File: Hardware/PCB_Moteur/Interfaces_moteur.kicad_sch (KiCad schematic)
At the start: 53 parts, among them J10 BM03B-GHS-TBT, J12 BM03B-GHS-TBT, J13 Conn_01x02, J14 Conn_01x02, J15 Conn_01x02, J16 Conn_01x02, J17 Conn_01x02, J2 Conn_01x02, J3 Conn_01x02, J4 Conn_01x02, J5 Conn_01x02, J6 BM03B-GHS-TBT, J9 BM03B-GHS-TBT, U1 MCP1802T-5002I/OT, U4 LSF0204PWR, U8 ISOW1044

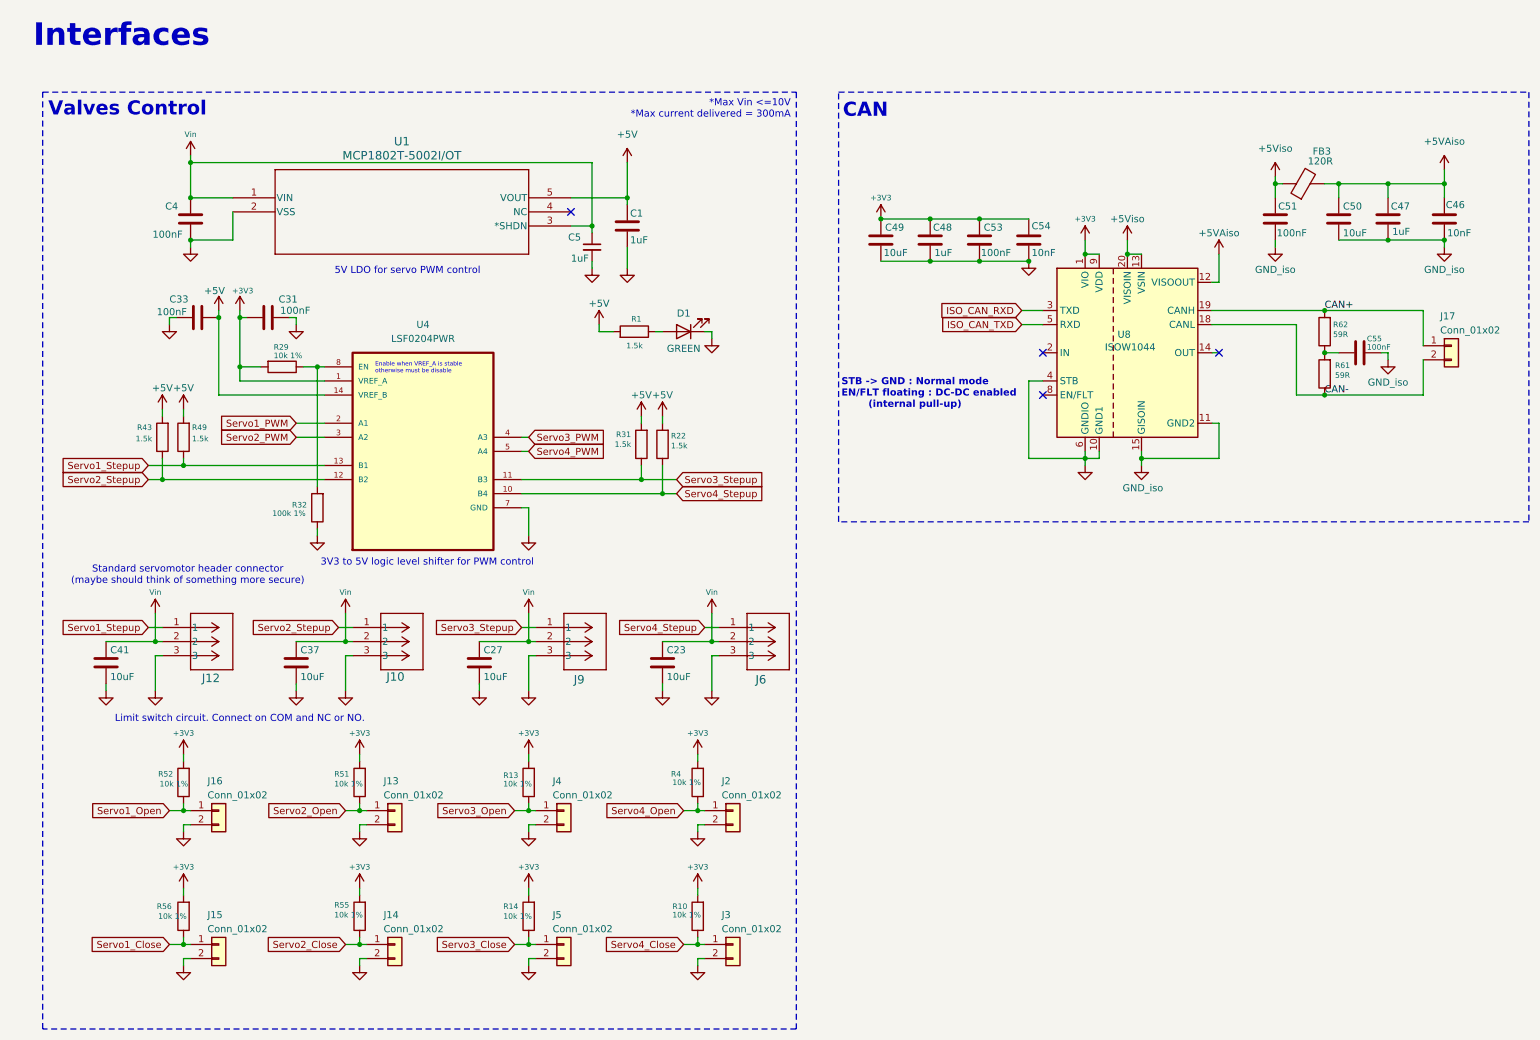
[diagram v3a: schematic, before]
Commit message: wip(moteur): add jack connector + fix dump valve
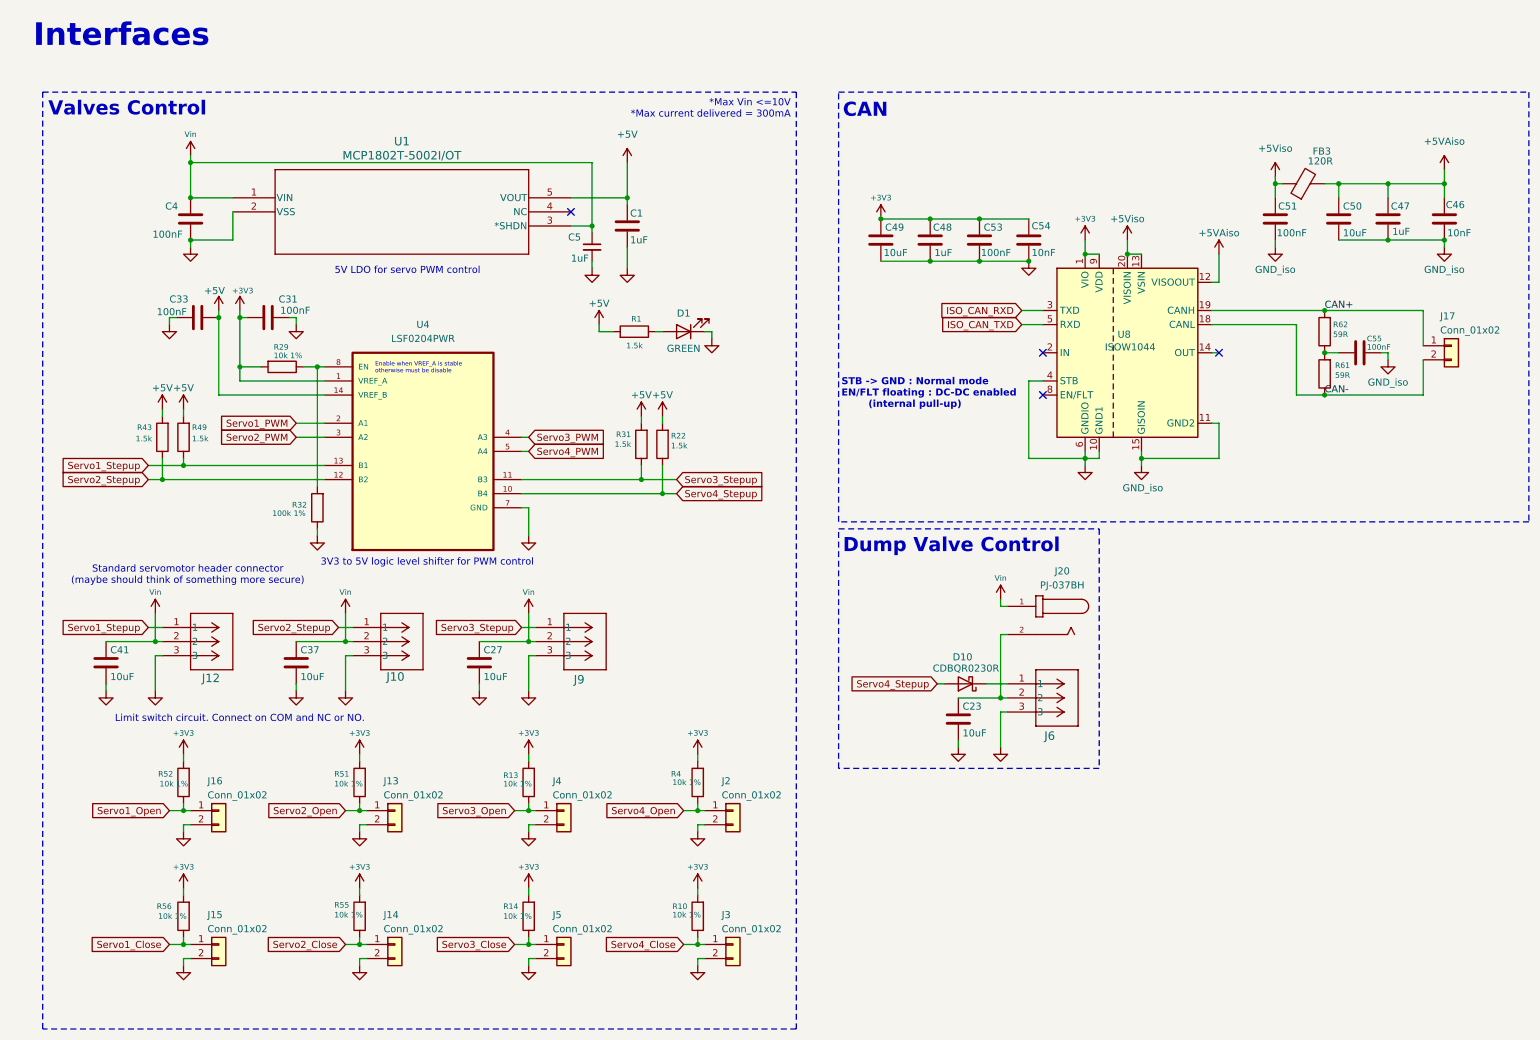
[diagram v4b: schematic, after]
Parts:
- added D10: CDBQR0230R, Diode_SMD:D_0603_1608Metric, symbol Diode:BAT54J
- added J20: PJ-037BH, pcb_moteur:SAMESKY_PJ-037BH, symbol pcb_moteur:PJ-037BH
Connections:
- net Servo4_Stepup: now also D10.2 (A); no longer J6.1
- net Vin: now also J20.1; no longer C23.1, J6.2
- new net: C23.1, J20.2, J6.2
- new net: D10.1 (K), J6.1
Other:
- note added: "Dump Valve Control"
- moved on the sheet: C23, J6

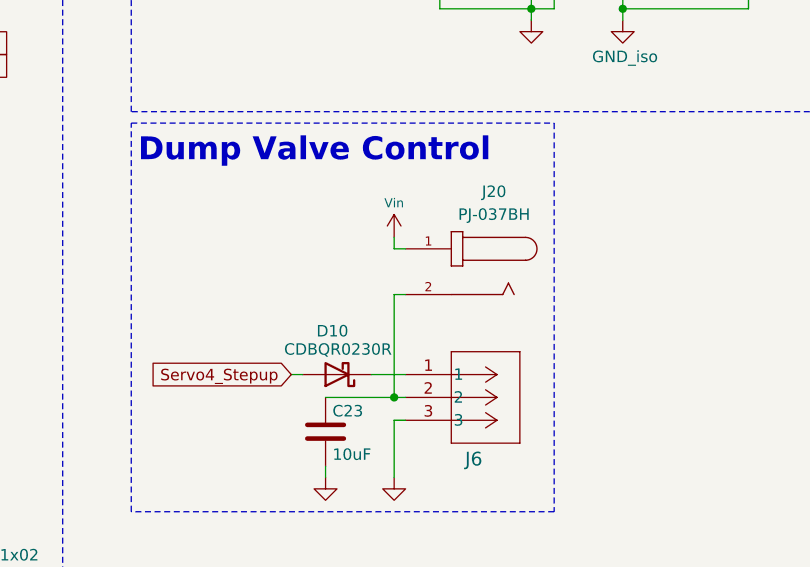
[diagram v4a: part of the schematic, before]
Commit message: Fix : connect all nets and fix dump valve kill
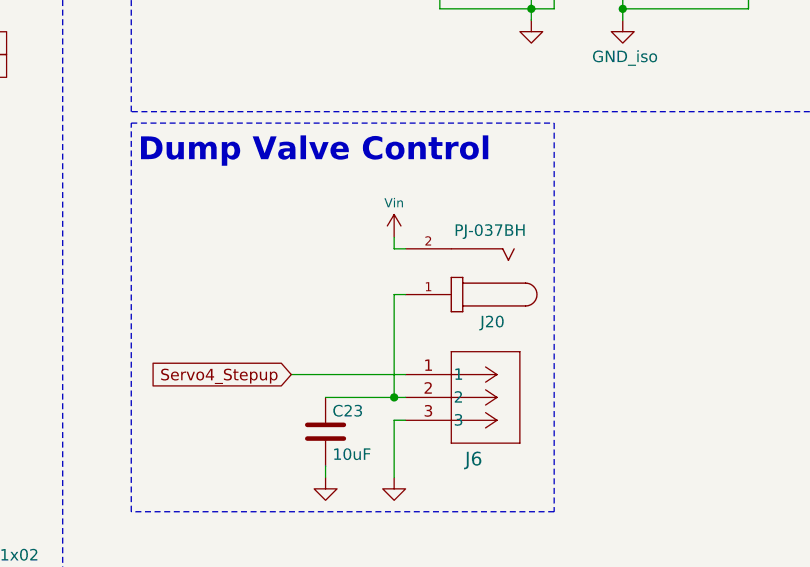
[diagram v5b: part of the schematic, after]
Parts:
- removed D10: CDBQR0230R, Diode_SMD:D_0603_1608Metric, symbol Diode:BAT54J
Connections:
- net Servo4_Stepup: now also J6.1
- net Vin: now also J20.2; no longer J20.1
- net at C23.1, J6.2: now also J20.1; no longer J20.2
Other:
- moved on the sheet: J20
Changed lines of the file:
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@@
 	(wire
 		(pts
+			(xy 187.96 119.38) (xy 189.23 119.38)
+		)
+		(stroke
+			(width 0)
+			(type default)
+		)
+	)
+	(wire
+		(pts
 			(xy 102.87 128.27) (xy 102.87 134.62)
 		)
@@
 	(wire
 		(pts
+			(xy 187.96 124.46) (xy 189.23 124.46)
+		)
+		(stroke
+			(width 0)
+			(type default)
+		)
+	)
+	(wire
+		(pts
 			(xy 36.83 125.73) (xy 35.56 125.73)
 		)
@@
 	(wire
 		(pts
-			(xy 189.23 124.46) (xy 187.96 124.46)
-		)
-		(stroke
-			(width 0)
-			(type default)
-		)
-	)
-	(wire
-		(pts
 			(xy 73.66 182.88) (xy 72.39 182.88)
 		)
@@
 	(wire
 		(pts
-			(xy 176.53 133.35) (xy 177.8 133.35)
+			(xy 176.53 133.35) (xy 189.23 133.35)
 		)
 		(stroke
@@
 	(wire
 		(pts
-			(xy 187.96 119.38) (xy 189.23 119.38)
-		)
-		(stroke
-			(width 0)
-			(type default)
-		)
-	)
-	(wire
-		(pts
 			(xy 46.99 67.31) (xy 46.99 81.28)
 		)
@@
 	(wire
 		(pts
-			(xy 185.42 133.35) (xy 189.23 133.35)
-		)
-		(stroke
-			(width 0)
-			(type default)
-		)
-	)
-	(wire
-		(pts
 			(xy 102.87 156.21) (xy 102.87 154.94)
 		)
@@
 	(symbol
 		(lib_id "pcb_moteur:PJ-037BH")
-		(at 194.31 121.92 0)
-		(mirror y)
+		(at 194.31 121.92 180)
 		(unit 1)
 		(exclude_from_sim no)
@@
 		(dnp no)
 		(property "Reference" "J20"
-			(at 199.0697 113.03 0)
+			(at 198.882 127.508 0)
 			(effects
 				(font
@@
 		)
 		(property "Value" "PJ-037BH"
-			(at 199.0697 115.57 0)
+			(at 198.628 117.348 0)
 			(effects
 				(font
@@
 					(unit 1)
 				)
-			)
-		)
-	)
-	(symbol
-		(lib_id "Diode:BAT54J")
-		(at 181.61 133.35 180)
-		(unit 1)
-		(exclude_from_sim no)
-		(in_bom yes)
-		(on_board yes)
-		(dnp no)
-		(property "Reference" "D10"
-			(at 182.88 128.524 0)
-			(effects
-				(font
-					(size 1.27 1.27)
-				)
-				(justify left)
-			)
-		)
-		(property "Value" "CDBQR0230R"
-			(at 187.706 130.556 0)
-			(effects
-				(font
-					(size 1.27 1.27)
-				)
-				(justify left)
-			)
-		)
-		(property "Footprint" "Diode_SMD:D_0603_1608Metric"
-			(at 181.61 128.905 0)
-			(effects
-				(font
-					(size 1.27 1.27)
-				)
-				(hide yes)
-			)
-		)
-		(property "Datasheet" "https://www.digikey.ca/en/products/detail/bourns-inc/CD0603-B0340R/7796828"
-			(at 181.61 133.35 0)
-			(effects
-				(font
-					(size 1.27 1.27)
-				)
-				(hide yes)
-			)
-		)
-		(property "Description" "30V 200mA Schottky diode, SOD-323F"
-			(at 181.61 133.35 0)
-			(effects
-				(font
-					(size 1.27 1.27)
-				)
-				(hide yes)
-			)
-		)
-		(property "DigiKey_Part_Number" "CD0603-B0340RCT-ND"
-			(at 181.61 133.35 90)
-			(effects
-				(font
-					(size 1.27 1.27)
-				)
-				(hide yes)
-			)
-		)
-		(property "Manufacturer_Part_Number" "CD0603-B0340R"
-			(at 181.61 133.35 90)
-			(effects
-				(font
-					(size 1.27 1.27)
-				)
-				(hide yes)
-			)
-		)
-		(pin "2"
-		)
-		(pin "1"
-		)
-		(instances
-			(project "PCB_moteur"
-				(path "/b0d87684-7b1c-41d8-8358-755aa327573e/a8ed0c04-b51e-4eec-84d1-0b2303d57d27"
-					(reference "D10")
-					(unit 1)
-				)

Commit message: Fix : servo side connectors
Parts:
- J10, J12, J6, J9: footprint pcb_moteur:CONN_BM03B-GHS-TBT_JST -> CONN_BM03B-GHS-TBT_JST; DigiKey_Part_Number - -> 455-SM03B-GHS-TBCT-ND; Manufacturer_Part_Number - -> SM03B-GHS-TB
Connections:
- net Vin: now also J10.4 (Case), J12.4 (Case), J9.4 (Case)
- no-connect marks 4 -> 5

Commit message: fix : add polyfuses and fix 90 deg servo connectors
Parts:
- J10, J12, J6, J9: footprint CONN_BM03B-GHS-TBT_JST -> pcb_moteur:JST_SM03B-GHS-TB
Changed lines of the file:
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@@
 			)
 		)
-		(property "Footprint" "CONN_BM03B-GHS-TBT_JST"
+		(property "Footprint" "pcb_moteur:JST_SM03B-GHS-TB"
 			(at 104.14 123.19 0)
 			(effects
@@
 			)
 		)
-		(property "Footprint" "CONN_BM03B-GHS-TBT_JST"
+		(property "Footprint" "pcb_moteur:JST_SM03B-GHS-TB"
 			(at 36.83 123.19 0)
 			(effects
@@
 			)
 		)
-		(property "Footprint" "CONN_BM03B-GHS-TBT_JST"
+		(property "Footprint" "pcb_moteur:JST_SM03B-GHS-TB"
 			(at 189.23 133.35 0)
 			(effects
@@
 			)
 		)
-		(property "Footprint" "CONN_BM03B-GHS-TBT_JST"
+		(property "Footprint" "pcb_moteur:JST_SM03B-GHS-TB"
 			(at 71.12 123.19 0)
 			(effects

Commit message: fix : BOM errors, change cutoff freq for moteur, minor fixes for GSE
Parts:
- C1, C47, C48, C5: DigiKey_Part_Number 399-C0603C105K4RACTUCT-ND -> 1276-1029-1-ND; Manufacturer_Part_Number C0603C105K4RACTU -> CL21B105KBFNNNE
- J20: Manufacturer_Part_Number (none) -> PJ-037BH
- R1, R22, R31, R43, R49: DigiKey_Part_Number P1.5KDBCT-ND -> 311-1.50KCRCT-ND; Manufacturer_Part_Number ERA-3AEB152V -> RC0805FR-071K5L
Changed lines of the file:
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@@
 			)
 		)
-		(property "Datasheet" "https://www.digikey.ca/en/products/detail/kemet/C0603C105K4RACTU/2199788"
+		(property "Datasheet" "https://www.digikey.ca/en/products/detail/samsung-electro-mechanics/CL21B105KBFNNNE/3886687"
 			(at 114.3 54.61 0)
 			(effects
@@
 			)
 		)
-		(property "DigiKey_Part_Number" "399-C0603C105K4RACTUCT-ND"
+		(property "DigiKey_Part_Number" "1276-1029-1-ND"
 			(at 114.3 54.61 0)
 			(effects
@@
 			)
 		)
-		(property "Manufacturer_Part_Number" "C0603C105K4RACTU"
+		(property "Manufacturer_Part_Number" "CL21B105KBFNNNE"
 			(at 114.3 54.61 0)
 			(effects
@@
 			)
 		)
+		(property "Manufacturer_Part_Number" "PJ-037BH"
+			(at 194.31 121.92 0)
+			(effects
+				(font
+					(size 1.27 1.27)
+				)
+				(hide yes)
+			)
+		)
 		(pin "2"
 		)
@@
 			)
 		)
-		(property "Datasheet" "399-C0603C103K5RACTUCT-ND"
+		(property "Datasheet" "https://www.digikey.ca/en/products/detail/kemet/C0603C103K5RACTU/411090?s=N4IgTCBcDaIMwE4EFoDCAGAbOuqCMOA0gKwBKAgqgCoCq1yAcgCIgC6AvkA"
 			(at 267.97 49.53 0)
 			(effects
@@
 			)
 		)
-		(property "Datasheet" "399-C0603C103K5RACTUCT-ND"
+		(property "Datasheet" "https://www.digikey.ca/en/products/detail/kemet/C0603C103K5RACTU/411090?s=N4IgTCBcDaIMwE4EFoDCAGAbOuqCMOA0gKwBKAgqgCoCq1yAcgCIgC6AvkA"
 			(at 193.04 53.34 0)
 			(effects
@@
 			)
 		)
-		(property "Datasheet" "BM03B-GHS-TBT"
+		(property "Datasheet" "https://www.digikey.ca/en/products/detail/jst-sales-america-inc/SM03B-GHS-TB/807787?s=N4IgTCBcDaICwFYEFoDKBZADAZgELIHEAJVZAFVwGEzkA5AERAF0BfIA"
 			(at 104.14 123.19 0)
 			(effects
@@
 			)
 		)
-		(property "Datasheet" "https://www.digikey.ca/en/products/detail/panasonic-electronic-components/ERA-3AEB152V/1465858"
+		(property "Datasheet" "https://www.digikey.ca/en/products/detail/yageo/RC0805FR-071K5L/727496"
 			(at 127 90.17 0)
 			(effects
@@
 			)
 		)
-		(property "DigiKey_Part_Number" "P1.5KDBCT-ND"
+		(property "DigiKey_Part_Number" "311-1.50KCRCT-ND"
 			(at 127 90.17 0)
 			(effects
@@
 			)
 		)
-		(property "Manufacturer_Part_Number" "ERA-3AEB152V"
+		(property "Manufacturer_Part_Number" "RC0805FR-071K5L"
 			(at 127 90.17 0)
 			(effects
@@
 			)
 		)
-		(property "Datasheet" "BM03B-GHS-TBT"
+		(property "Datasheet" "https://www.digikey.ca/en/products/detail/jst-sales-america-inc/SM03B-GHS-TB/807787?s=N4IgTCBcDaICwFYEFoDKBZADAZgELIHEAJVZAFVwGEzkA5AERAF0BfIA"
 			(at 36.83 123.19 0)
 			(effects
@@
 			)
 		)
-		(property "Datasheet" "BM03B-GHS-TBT"
+		(property "Datasheet" "https://www.digikey.ca/en/products/detail/jst-sales-america-inc/SM03B-GHS-TB/807787?s=N4IgTCBcDaICwFYEFoDKBZADAZgELIHEAJVZAFVwGEzkA5AERAF0BfIA"
 			(at 189.23 133.35 0)
 			(effects
@@
 			)
 		)
-		(property "Datasheet" "https://www.digikey.ca/en/products/detail/panasonic-electronic-components/ERA-3AEB152V/1465858"
+		(property "Datasheet" "https://www.digikey.ca/en/products/detail/yageo/RC0805FR-071K5L/727496"
 			(at 40.64 88.9 0)
 			(effects
@@
 			)
 		)
-		(property "DigiKey_Part_Number" "P1.5KDBCT-ND"
+		(property "DigiKey_Part_Number" "311-1.50KCRCT-ND"
 			(at 40.64 88.9 0)
 			(effects
@@
 			)
 		)
-		(property "Manufacturer_Part_Number" "ERA-3AEB152V"
+		(property "Manufacturer_Part_Number" "RC0805FR-071K5L"
 			(at 40.64 88.9 0)
 			(effects
@@
 			)
 		)
-		(property "Datasheet" "https://www.digikey.ca/en/products/detail/kemet/C0603C105K4RACTU/2199788"
+		(property "Datasheet" "https://www.digikey.ca/en/products/detail/samsung-electro-mechanics/CL21B105KBFNNNE/3886687"
 			(at 120.65 50.8 0)
 			(effects
@@
 			)
 		)
-		(property "DigiKey_Part_Number" "399-C0603C105K4RACTUCT-ND"
+		(property "DigiKey_Part_Number" "1276-1029-1-ND"
 			(at 120.65 50.8 0)
 			(effects
@@
 			)
 		)
-		(property "Manufacturer_Part_Number" "C0603C105K4RACTU"
+		(property "Manufacturer_Part_Number" "CL21B105KBFNNNE"
 			(at 120.65 50.8 0)
 			(effects
@@
 			)
 		)
-		(property "Datasheet" "BM03B-GHS-TBT"
+		(property "Datasheet" "https://www.digikey.ca/en/products/detail/jst-sales-america-inc/SM03B-GHS-TB/807787?s=N4IgTCBcDaICwFYEFoDKBZADAZgELIHEAJVZAFVwGEzkA5AERAF0BfIA"
 			(at 71.12 123.19 0)
 			(effects
@@
 			)
 		)
-		(property "Datasheet" "https://www.digikey.ca/en/products/detail/kemet/C0603C105K4RACTU/2199788"
+		(property "Datasheet" "https://www.digikey.ca/en/products/detail/samsung-electro-mechanics/CL21B105KBFNNNE/3886687"
 			(at 257.81 49.53 0)
 			(effects
@@
 			)
 		)
-		(property "DigiKey_Part_Number" "399-C0603C105K4RACTUCT-ND"
+		(property "DigiKey_Part_Number" "1276-1029-1-ND"
 			(at 257.81 49.53 0)
 			(effects
@@
 			)
 		)
-		(property "Manufacturer_Part_Number" "C0603C105K4RACTU"
+		(property "Manufacturer_Part_Number" "CL21B105KBFNNNE"
 			(at 257.81 49.53 0)
 			(effects
@@
 			)
 		)
-		(property "Datasheet" "https://www.digikey.ca/en/products/detail/kemet/C0603C105K4RACTU/2199788"
+		(property "Datasheet" "https://www.digikey.ca/en/products/detail/samsung-electro-mechanics/CL21B105KBFNNNE/3886687"
 			(at 175.26 53.34 0)
 			(effects
@@
 			)
 		)
-		(property "DigiKey_Part_Number" "399-C0603C105K4RACTUCT-ND"
+		(property "DigiKey_Part_Number" "1276-1029-1-ND"
 			(at 175.26 53.34 0)
 			(effects
@@
 			)
 		)
-		(property "Manufacturer_Part_Number" "C0603C105K4RACTU"
+		(property "Manufacturer_Part_Number" "CL21B105KBFNNNE"
 			(at 175.26 53.34 0)
 			(effects
@@
 			)
 		)
-		(property "Datasheet" "https://www.digikey.ca/en/products/detail/panasonic-electronic-components/ERA-3AEB152V/1465858"
+		(property "Datasheet" "https://www.digikey.ca/en/products/detail/yageo/RC0805FR-071K5L/727496"
 			(at 36.83 88.9 0)
 			(effects
@@
 			)
 		)
-		(property "DigiKey_Part_Number" "P1.5KDBCT-ND"
+		(property "DigiKey_Part_Number" "311-1.50KCRCT-ND"
 			(at 36.83 88.9 0)
 			(effects
@@
 			)
 		)
-		(property "Manufacturer_Part_Number" "ERA-3AEB152V"
+		(property "Manufacturer_Part_Number" "RC0805FR-071K5L"
 			(at 36.83 88.9 0)
 			(effects
@@
 			)
 		)
-		(property "Datasheet" "https://www.digikey.ca/en/products/detail/panasonic-electronic-components/ERA-3AEB152V/1465858"
+		(property "Datasheet" "https://www.digikey.ca/en/products/detail/yageo/RC0805FR-071K5L/727496"
 			(at 121.92 69.85 0)
 			(effects
@@
 			)
 		)
-		(property "DigiKey_Part_Number" "P1.5KDBCT-ND"
+		(property "DigiKey_Part_Number" "311-1.50KCRCT-ND"
 			(at 121.92 69.85 90)
 			(effects
@@
 			)
 		)
-		(property "Manufacturer_Part_Number" "ERA-3AEB152V"
+		(property "Manufacturer_Part_Number" "RC0805FR-071K5L"
 			(at 121.92 69.85 90)
 			(effects
@@
 			)
 		)
-		(property "Datasheet" "https://www.digikey.ca/en/products/detail/panasonic-electronic-components/ERA-3AEB152V/1465858"
+		(property "Datasheet" "https://www.digikey.ca/en/products/detail/yageo/RC0805FR-071K5L/727496"
 			(at 123.19 90.17 0)
 			(effects
@@
 			)
 		)
-		(property "DigiKey_Part_Number" "P1.5KDBCT-ND"
+		(property "DigiKey_Part_Number" "311-1.50KCRCT-ND"
 			(at 123.19 90.17 0)
 			(effects
@@
 			)
 		)
-		(property "Manufacturer_Part_Number" "ERA-3AEB152V"
+		(property "Manufacturer_Part_Number" "RC0805FR-071K5L"
 			(at 123.19 90.17 0)
 			(effects
